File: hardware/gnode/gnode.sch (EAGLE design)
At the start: 25 parts, among them IC1 HTU21D, U1 ATMEGA328P_TQFP

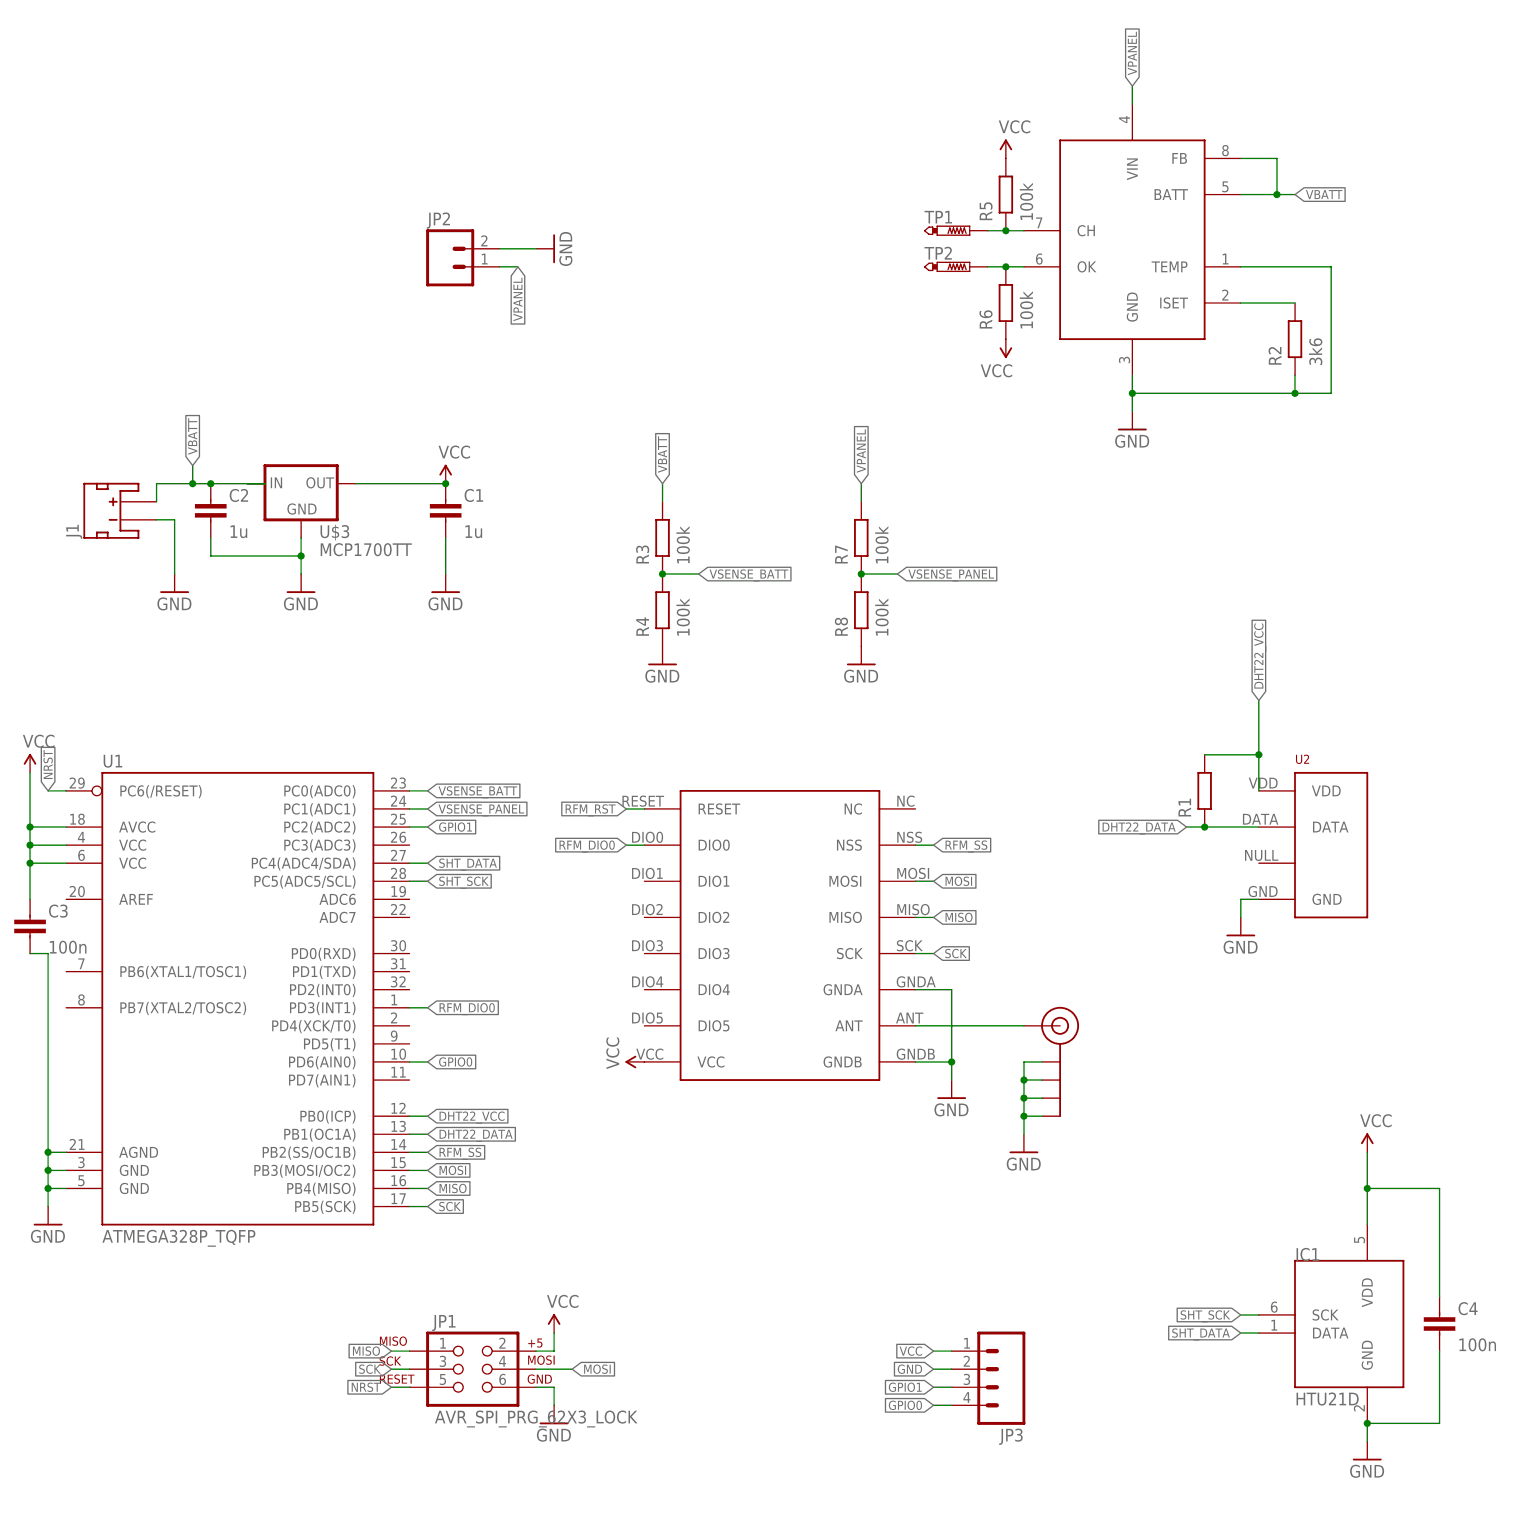
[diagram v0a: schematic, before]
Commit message: added RC for rain sensing. part numbers on silk
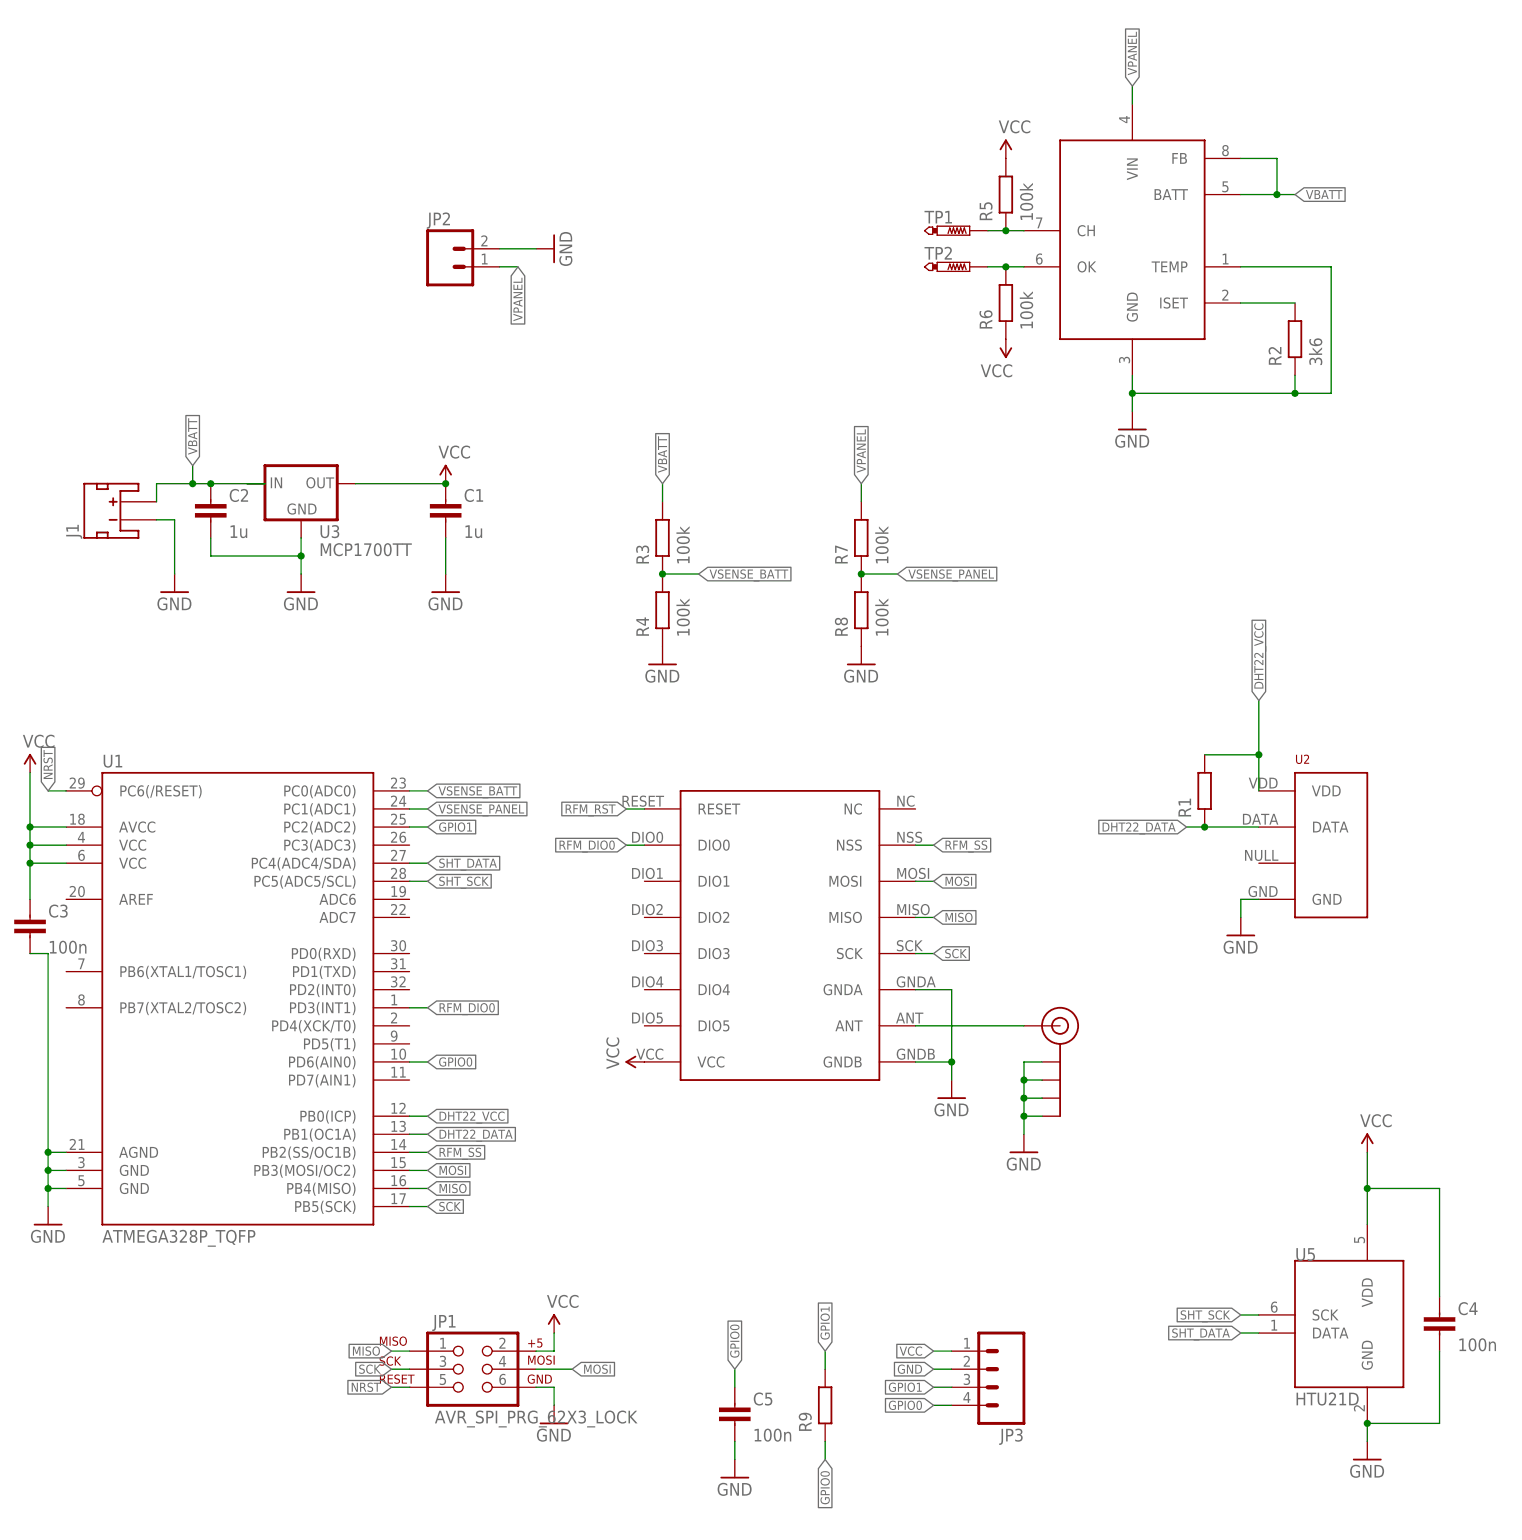
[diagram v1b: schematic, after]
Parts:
- added C5: 100n, passives-7351:CAPACITOR0603-N
- added R9: (no value), passives-7351:RESISTOR0603-N
- renumbered IC1 to U5, U$3 to U3, U$4 to U4
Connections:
- net GND: now also C5.2
- net GPIO0: now also C5.1, R9.P$1
- net GPIO1: now also R9.P$2
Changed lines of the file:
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@@
 <part name="SUPPLY3" library="SparkFun-Aesthetics" deviceset="VCC" device=""/>
 <part name="GND7" library="SparkFun-Aesthetics" deviceset="GND" device=""/>
-<part name="IC1" library="Mine" deviceset="HTU21D" device=""/>
+<part name="U5" library="Mine" deviceset="HTU21D" device=""/>
 <part name="SUPPLY4" library="SparkFun-Aesthetics" deviceset="VCC" device=""/>
 <part name="GND8" library="SparkFun-Aesthetics" deviceset="GND" device=""/>
@@
 <part name="SUPPLY5" library="SparkFun-Aesthetics" deviceset="VCC" device=""/>
 <part name="GND9" library="SparkFun-Aesthetics" deviceset="GND" device=""/>
-<part name="U$3" library="dtb" deviceset="MCP1700" device="TT"/>
+<part name="U3" library="dtb" deviceset="MCP1700" device="TT"/>
 <part name="C2" library="passives-7351" deviceset="CAPACITOR" device="0603-N" value="1u"/>
-<part name="U$4" library="jonsowman" deviceset="CN3083" device=""/>
+<part name="U4" library="jonsowman" deviceset="CN3083" device=""/>
 <part name="JP2" library="Mine" deviceset="M02" device="PTH"/>
 <part name="GND10" library="SparkFun-Aesthetics" deviceset="GND" device=""/>
@@
 <part name="JP3" library="SparkFun-Connectors" deviceset="M04" device="PTH"/>
 <part name="C4" library="passives-7351" deviceset="CAPACITOR" device="0603-N" value="100n"/>
+<part name="R9" library="passives-7351" deviceset="RESISTOR" device="0603-N"/>
+<part name="C5" library="passives-7351" deviceset="CAPACITOR" device="0603-N" value="100n"/>
+<part name="GND14" library="SparkFun-Aesthetics" deviceset="GND" device=""/>
 </parts>
 <sheets>
@@
 <instance part="SUPPLY3" gate="G$1" x="17.78" y="109.22"/>
 <instance part="GND7" gate="1" x="17.78" y="93.98"/>
-<instance part="IC1" gate="G$1" x="142.24" y="-10.16"/>
+<instance part="U5" gate="G$1" x="142.24" y="-10.16"/>
 <instance part="SUPPLY4" gate="G$1" x="147.32" y="15.24"/>
 <instance part="GND8" gate="1" x="147.32" y="-27.94"/>
@@
 <instance part="SUPPLY5" gate="G$1" x="33.02" y="-10.16"/>
 <instance part="GND9" gate="1" x="33.02" y="-22.86"/>
-<instance part="U$3" gate="G$1" x="-2.54" y="109.22"/>
+<instance part="U3" gate="G$1" x="-2.54" y="109.22"/>
 <instance part="C2" gate="G$1" x="-15.24" y="106.68"/>
-<instance part="U$4" gate="G$1" x="114.3" y="149.86"/>
+<instance part="U4" gate="G$1" x="114.3" y="149.86"/>
 <instance part="JP2" gate="G$1" x="17.78" y="139.7"/>
 <instance part="GND10" gate="1" x="33.02" y="142.24" rot="R90"/>
@@
 <instance part="R8" gate="G$1" x="76.2" y="91.44" rot="R90"/>
 <instance part="U2" gate="G$1" x="142.24" y="58.42"/>
-<instance part="C3" gate="G$1" x="-40.64" y="48.26"/>
+<instance part="C3" gate="G$1" x="-40.64" y="48.26" smashed="yes">
+<attribute name="NAME" x="-38.1" y="48.26" size="1.778" layer="95"/>
+<attribute name="VALUE" x="-38.1" y="43.18" size="1.778" layer="96"/>
+</instance>
 <instance part="JP3" gate="G$1" x="93.98" y="-15.24" rot="R180"/>
 <instance part="C4" gate="G$1" x="157.48" y="-7.62"/>
+<instance part="R9" gate="G$1" x="71.12" y="-20.32" rot="R90"/>
+<instance part="C5" gate="G$1" x="58.42" y="-20.32" smashed="yes">
+<attribute name="NAME" x="60.96" y="-20.32" size="1.778" layer="95"/>
+<attribute name="VALUE" x="60.96" y="-25.4" size="1.778" layer="96"/>
+</instance>
+<instance part="GND14" gate="1" x="58.42" y="-30.48"/>
 </instances>
 <busses>
@@
 </segment>
 <segment>
-<pinref part="IC1" gate="G$1" pin="GND"/>
+<pinref part="U5" gate="G$1" pin="GND"/>
 <pinref part="GND8" gate="1" pin="GND"/>
 <wire x1="147.32" y1="-22.86" x2="147.32" y2="-25.4" width="0.1524" layer="91"/>
@@
 </segment>
 <segment>
-<pinref part="U$3" gate="G$1" pin="GND"/>
+<pinref part="U3" gate="G$1" pin="GND"/>
 <pinref part="GND6" gate="1" pin="GND"/>
 <wire x1="-2.54" y1="101.6" x2="-2.54" y2="99.06" width="0.1524" layer="91"/>
@@
 </segment>
 <segment>
-<pinref part="U$4" gate="G$1" pin="GND"/>
+<pinref part="U4" gate="G$1" pin="GND"/>
 <pinref part="GND11" gate="1" pin="GND"/>
 <wire x1="114.3" y1="124.46" x2="114.3" y2="121.92" width="0.1524" layer="91"/>
@@
 <wire x1="137.16" y1="121.92" x2="114.3" y2="121.92" width="0.1524" layer="91"/>
 <junction x="114.3" y="121.92"/>
-<pinref part="U$4" gate="G$1" pin="TEMP"/>
+<pinref part="U4" gate="G$1" pin="TEMP"/>
 <wire x1="129.54" y1="139.7" x2="142.24" y2="139.7" width="0.1524" layer="91"/>
 <wire x1="142.24" y1="139.7" x2="142.24" y2="121.92" width="0.1524" layer="91"/>
@@
 <wire x1="88.9" y1="-15.24" x2="86.36" y2="-15.24" width="0.1524" layer="91"/>
 <label x="86.36" y="-15.24" size="1.27" layer="95" rot="R180" xref="yes"/>
+</segment>
+<segment>
+<pinref part="C5" gate="G$1" pin="2"/>
+<wire x1="58.42" y1="-25.4" x2="58.42" y2="-27.94" width="0.1524" layer="91"/>
+<pinref part="GND14" gate="1" pin="GND"/>
 </segment>
 </net>
@@
 <pinref part="SUPPLY3" gate="G$1" pin="VCC"/>
 <junction x="17.78" y="109.22"/>
-<pinref part="U$3" gate="G$1" pin="OUT"/>
+<pinref part="U3" gate="G$1" pin="OUT"/>
 </segment>
 <segment>
@@
 </segment>
 <segment>
-<pinref part="IC1" gate="G$1" pin="VDD"/>
+<pinref part="U5" gate="G$1" pin="VDD"/>
 <pinref part="SUPPLY4" gate="G$1" pin="VCC"/>
 <wire x1="147.32" y1="5.08" x2="147.32" y2="10.16" width="0.1524" layer="91"/>
@@
 <wire x1="-17.78" y1="109.22" x2="-22.86" y2="109.22" width="0.1524" layer="91"/>
 <wire x1="-22.86" y1="109.22" x2="-22.86" y2="106.68" width="0.1524" layer="91"/>
-<pinref part="U$3" gate="G$1" pin="IN"/>
+<pinref part="U3" gate="G$1" pin="IN"/>
 <pinref part="C2" gate="G$1" pin="1"/>
 <junction x="-15.24" y="109.22"/>
@@
 </segment>
 <segment>
-<pinref part="U$4" gate="G$1" pin="BATT"/>
+<pinref part="U4" gate="G$1" pin="BATT"/>
 <wire x1="129.54" y1="149.86" x2="134.62" y2="149.86" width="0.1524" layer="91"/>
 <label x="137.16" y="149.86" size="1.27" layer="95" xref="yes"/>
-<pinref part="U$4" gate="G$1" pin="FB"/>
+<pinref part="U4" gate="G$1" pin="FB"/>
 <wire x1="134.62" y1="149.86" x2="137.16" y2="149.86" width="0.1524" layer="91"/>
 <wire x1="129.54" y1="154.94" x2="134.62" y2="154.94" width="0.1524" layer="91"/>
@@
 <net name="SHT_SCK" class="0">
 <segment>
-<pinref part="IC1" gate="G$1" pin="SCK"/>
+<pinref part="U5" gate="G$1" pin="SCK"/>
 <wire x1="132.08" y1="-7.62" x2="129.54" y2="-7.62" width="0.1524" layer="91"/>
 <label x="129.54" y="-7.62" size="1.27" layer="95" rot="R180" xref="yes"/>
@@
 <net name="SHT_DATA" class="0">
 <segment>
-<pinref part="IC1" gate="G$1" pin="DATA"/>
+<pinref part="U5" gate="G$1" pin="DATA"/>
 <wire x1="132.08" y1="-10.16" x2="129.54" y2="-10.16" width="0.1524" layer="91"/>
 <label x="129.54" y="-10.16" size="1.27" layer="95" rot="R180" xref="yes"/>
@@
 <net name="N$4" class="0">
 <segment>
-<pinref part="U$4" gate="G$1" pin="ISET"/>
+<pinref part="U4" gate="G$1" pin="ISET"/>
 <pinref part="R2" gate="G$1" pin="P$2"/>
 <wire x1="129.54" y1="134.62" x2="137.16" y2="134.62" width="0.1524" layer="91"/>
@@
 <net name="N$2" class="0">
 <segment>
-<pinref part="U$4" gate="G$1" pin="CH"/>
+<pinref part="U4" gate="G$1" pin="CH"/>
 <pinref part="TP1" gate="G$1" pin="TP"/>
 <wire x1="93.98" y1="144.78" x2="96.52" y2="144.78" width="0.1524" layer="91"/>
@@
 <net name="N$5" class="0">
 <segment>
-<pinref part="U$4" gate="G$1" pin="OK"/>
+<pinref part="U4" gate="G$1" pin="OK"/>
 <pinref part="TP2" gate="G$1" pin="TP"/>
 <wire x1="93.98" y1="139.7" x2="96.52" y2="139.7" width="0.1524" layer="91"/>
@@
 </segment>
 <segment>
-<pinref part="U$4" gate="G$1" pin="VIN"/>
+<pinref part="U4" gate="G$1" pin="VIN"/>
 <wire x1="114.3" y1="162.56" x2="114.3" y2="165.1" width="0.1524" layer="91"/>
 <label x="114.3" y="165.1" size="1.27" layer="95" rot="R90" xref="yes"/>
@@
 <label x="86.36" y="-17.78" size="1.27" layer="95" rot="R180" xref="yes"/>
 </segment>
+<segment>
+<pinref part="R9" gate="G$1" pin="P$2"/>
+<wire x1="71.12" y1="-15.24" x2="71.12" y2="-12.7" width="0.1524" layer="91"/>
+<label x="71.12" y="-12.7" size="1.27" layer="95" rot="R90" xref="yes"/>
+</segment>
 </net>
 <net name="GPIO0" class="0">
@@
 <label x="86.36" y="-20.32" size="1.27" layer="95" rot="R180" xref="yes"/>
 </segment>
-</net>
+<segment>
+<pinref part="R9" gate="G$1" pin="P$1"/>
+<wire x1="71.12" y1="-25.4" x2="71.12" y2="-27.94" width="0.1524" layer="91"/>
+<label x="71.12" y="-27.94" size="1.27" layer="95" rot="R270" xref="yes"/>
+</segment>
+<segment>
+<pinref part="C5" gate="G$1" pin="1"/>
+<wire x1="58.42" y1="-17.78" x2="58.42" y2="-15.24" width="0.1524" layer="91"/>
+<label x="58.42" y="-15.24" size="1.27" layer="95" rot="R90" xref="yes"/>
+</segment>
+</net>

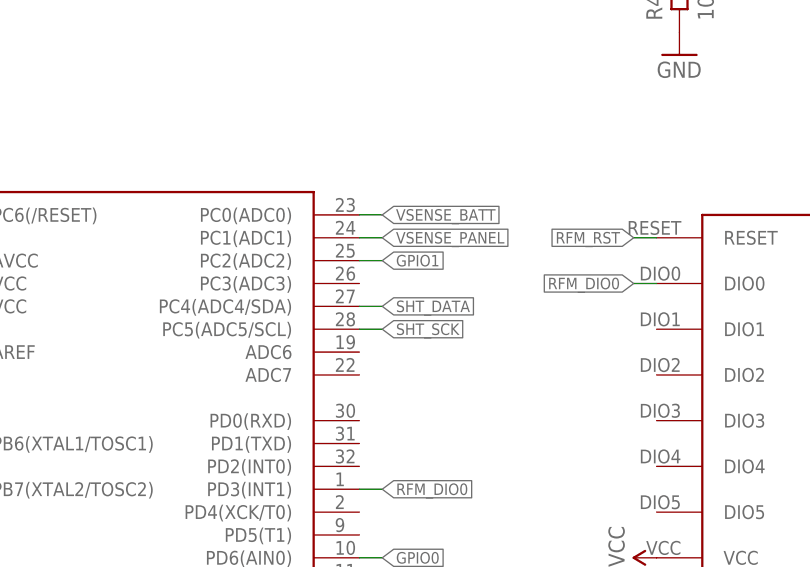
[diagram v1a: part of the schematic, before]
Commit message: ISET connected to ADC pin so we can calculate the charge current
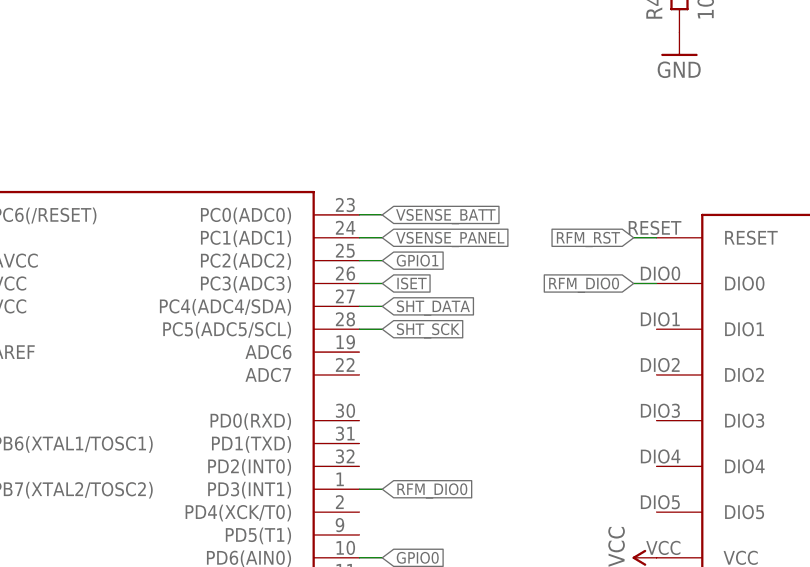
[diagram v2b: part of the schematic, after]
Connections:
- removed net N$4: R2.P$2, U4.ISET
- new net ISET: R2.P$2, U1.PC3(ADC3), U4.ISET
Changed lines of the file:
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@@
-</segment>
-</net>
-<net name="N$4" class="0">
-<segment>
-<pinref part="U4" gate="G$1" pin="ISET"/>
-<pinref part="R2" gate="G$1" pin="P$2"/>
-<wire x1="129.54" y1="134.62" x2="137.16" y2="134.62" width="0.1524" layer="91"/>
 </segment>
 </net>
@@
 </segment>
 </net>
+<net name="ISET" class="0">
+<segment>
+<pinref part="U1" gate="U$1" pin="PC3(ADC3)"/>
+<wire x1="12.7" y1="58.42" x2="15.24" y2="58.42" width="0.1524" layer="91"/>
+<label x="15.24" y="58.42" size="1.27" layer="95" xref="yes"/>
+</segment>
+<segment>
+<pinref part="U4" gate="G$1" pin="ISET"/>
+<pinref part="R2" gate="G$1" pin="P$2"/>
+<wire x1="129.54" y1="134.62" x2="137.16" y2="134.62" width="0.1524" layer="91"/>
+</segment>
+</net>
